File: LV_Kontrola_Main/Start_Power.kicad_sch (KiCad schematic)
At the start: 14 parts, among them U3 MCP1826T-ADJE_DC, U5 MCP1826T-ADJE_DC

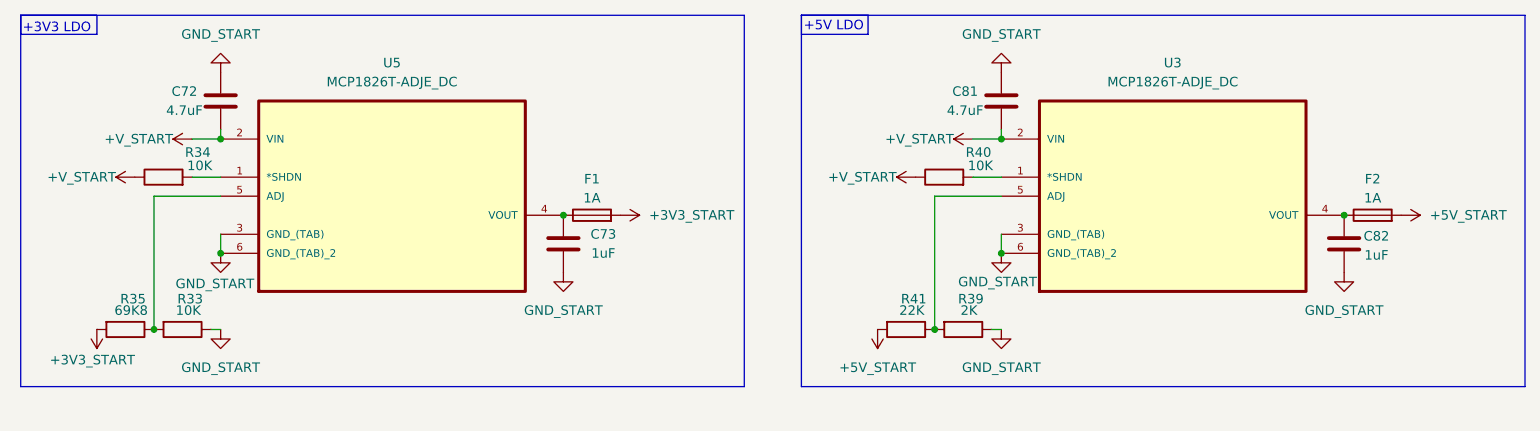
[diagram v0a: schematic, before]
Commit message: Changes to LV_Kontrola_Main
Added a lot to the schematic, fixed component libs, mics...
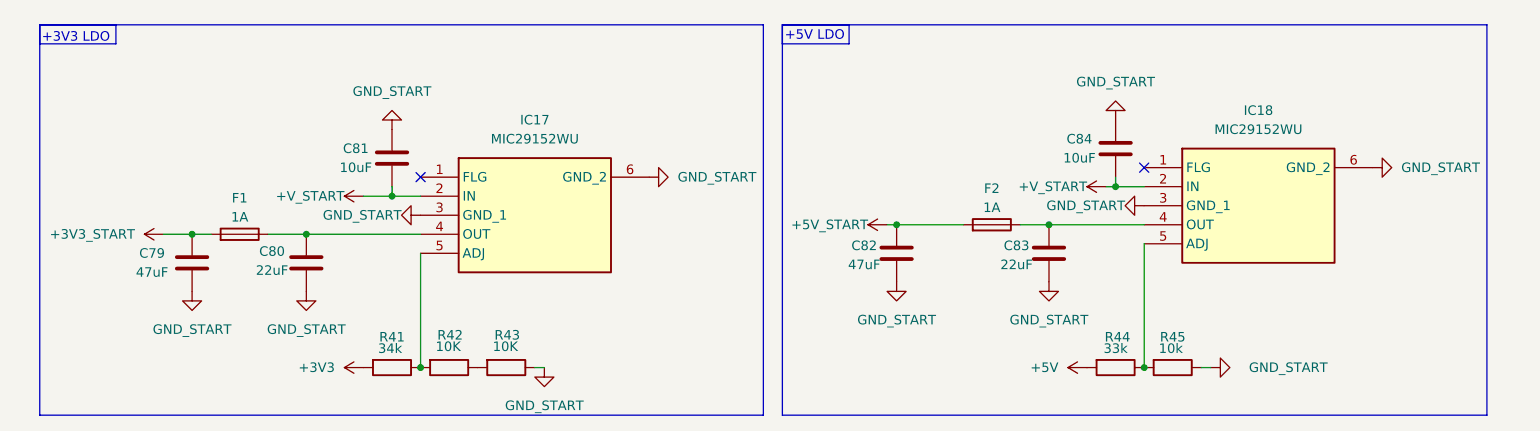
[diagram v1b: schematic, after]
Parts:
- removed C72: 4.7uF, symbol Device:C
- removed C73: 1uF, symbol Device:C
- removed R33, R34, R40: 10K, symbol Device:R
- removed R35: 69K8, symbol Device:R
- removed R39: 2K, symbol Device:R
- removed U3, U5: MCP1826T-ADJE_DC, MCP1826T-ADJE_DC:SOT230P700X180-6N, symbol MCP1826T-ADJE_DC:MCP1826T-ADJE_DC
- added C79: 47uF, Capacitor_SMD:C_1206_3216Metric_Pad1.33x1.80mm_HandSolder, symbol Device:C
- added C80, C83: 22uF, Capacitor_SMD:C_1206_3216Metric_Pad1.33x1.80mm_HandSolder, symbol Device:C
- added C84: 10uF, Capacitor_SMD:C_1206_3216Metric_Pad1.33x1.80mm_HandSolder, symbol Device:C
- added IC17, IC18: MIC29152WU, MIC29152WU:MIC29152WU, symbol MIC29152WU:MIC29152WU
- added R42, R43: 10K, Resistor_SMD:R_1206_3216Metric_Pad1.30x1.75mm_HandSolder, symbol Device:R
- added R44: 33k, Resistor_SMD:R_1206_3216Metric_Pad1.30x1.75mm_HandSolder, symbol Device:R
- added R45: 10k, Resistor_SMD:R_1206_3216Metric_Pad1.30x1.75mm_HandSolder, symbol Device:R
- C81: value 4.7uF -> 10uF; footprint (none) -> Capacitor_SMD:C_1206_3216Metric_Pad1.33x1.80mm_HandSolder; Purchase Place (none) -> https://eu.mouser.com/ProductDetail/KYOCERA-AVX/12066G106ZA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
- C82: value 1uF -> 47uF; footprint (none) -> Capacitor_SMD:C_1206_3216Metric_Pad1.33x1.80mm_HandSolder; Purchase Place (none) -> https://eu.mouser.com/ProductDetail/TAIYO-YUDEN/MLASJ319LB5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
- F1, F2: footprint (none) -> Fuse:Fuse_1206_3216Metric_Pad1.42x1.75mm_HandSolder; Purchase Place (none) -> https://eu.mouser.com/ProductDetail/Bourns/SF-1206S100-2?qs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
- R41: value 22K -> 34k; footprint (none) -> Resistor_SMD:R_1206_3216Metric_Pad1.30x1.75mm_HandSolder
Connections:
- net +3V3_START: now also C79.2
- net +5V_START: now also C82.2
- net +V_START: now also C84.2, IC17.2 (IN), IC18.2 (IN)
- net GND_START: now also C79.1, C80.1, C83.1, C84.1, IC17.3 (GND_1), IC17.6 (GND_2), IC18.3 (GND_1), IC18.6 (GND_2), R43.1, R45.1; no longer R41.1
- net at F2.1: now also C83.2, IC18.4 (OUT); no longer C82.2
- net +3V3: now reaches R41.2
- net at F1.1: now also C80.2, IC17.4 (OUT)
- new net: R42.1, R43.2
- new net: IC17.5 (ADJ), R41.1, R42.2
- new net: IC18.5 (ADJ), R44.1, R45.2
- new net +5V: R44.2
- no-connect marks 0 -> 2
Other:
- moved on the sheet: F2
